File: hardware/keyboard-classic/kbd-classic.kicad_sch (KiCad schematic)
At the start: 19 parts, among them J1 Controller, SW17 Line_Feed, SW32 @(OSI SL), SW34 Rubout (OSI Break), SW61 Power Light, SW9 Caps_Lock

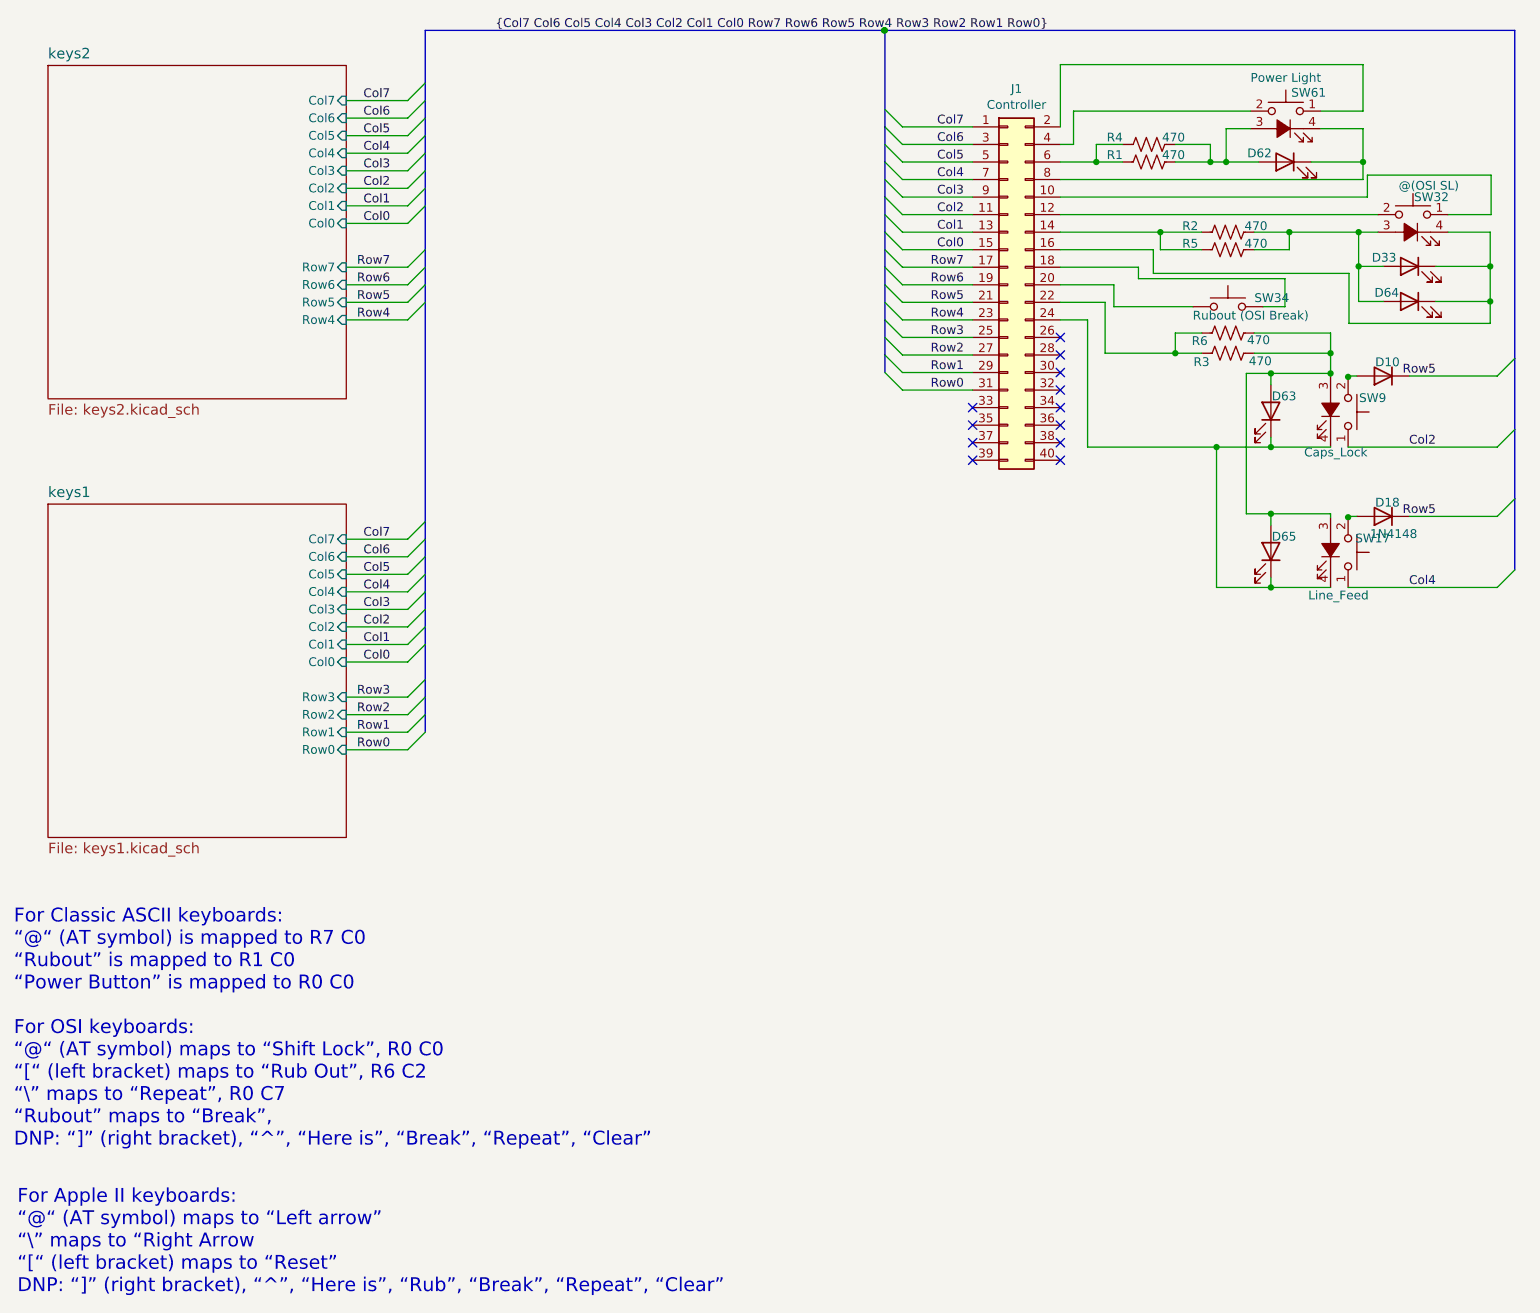
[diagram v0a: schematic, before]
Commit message: Add some mounting hardware
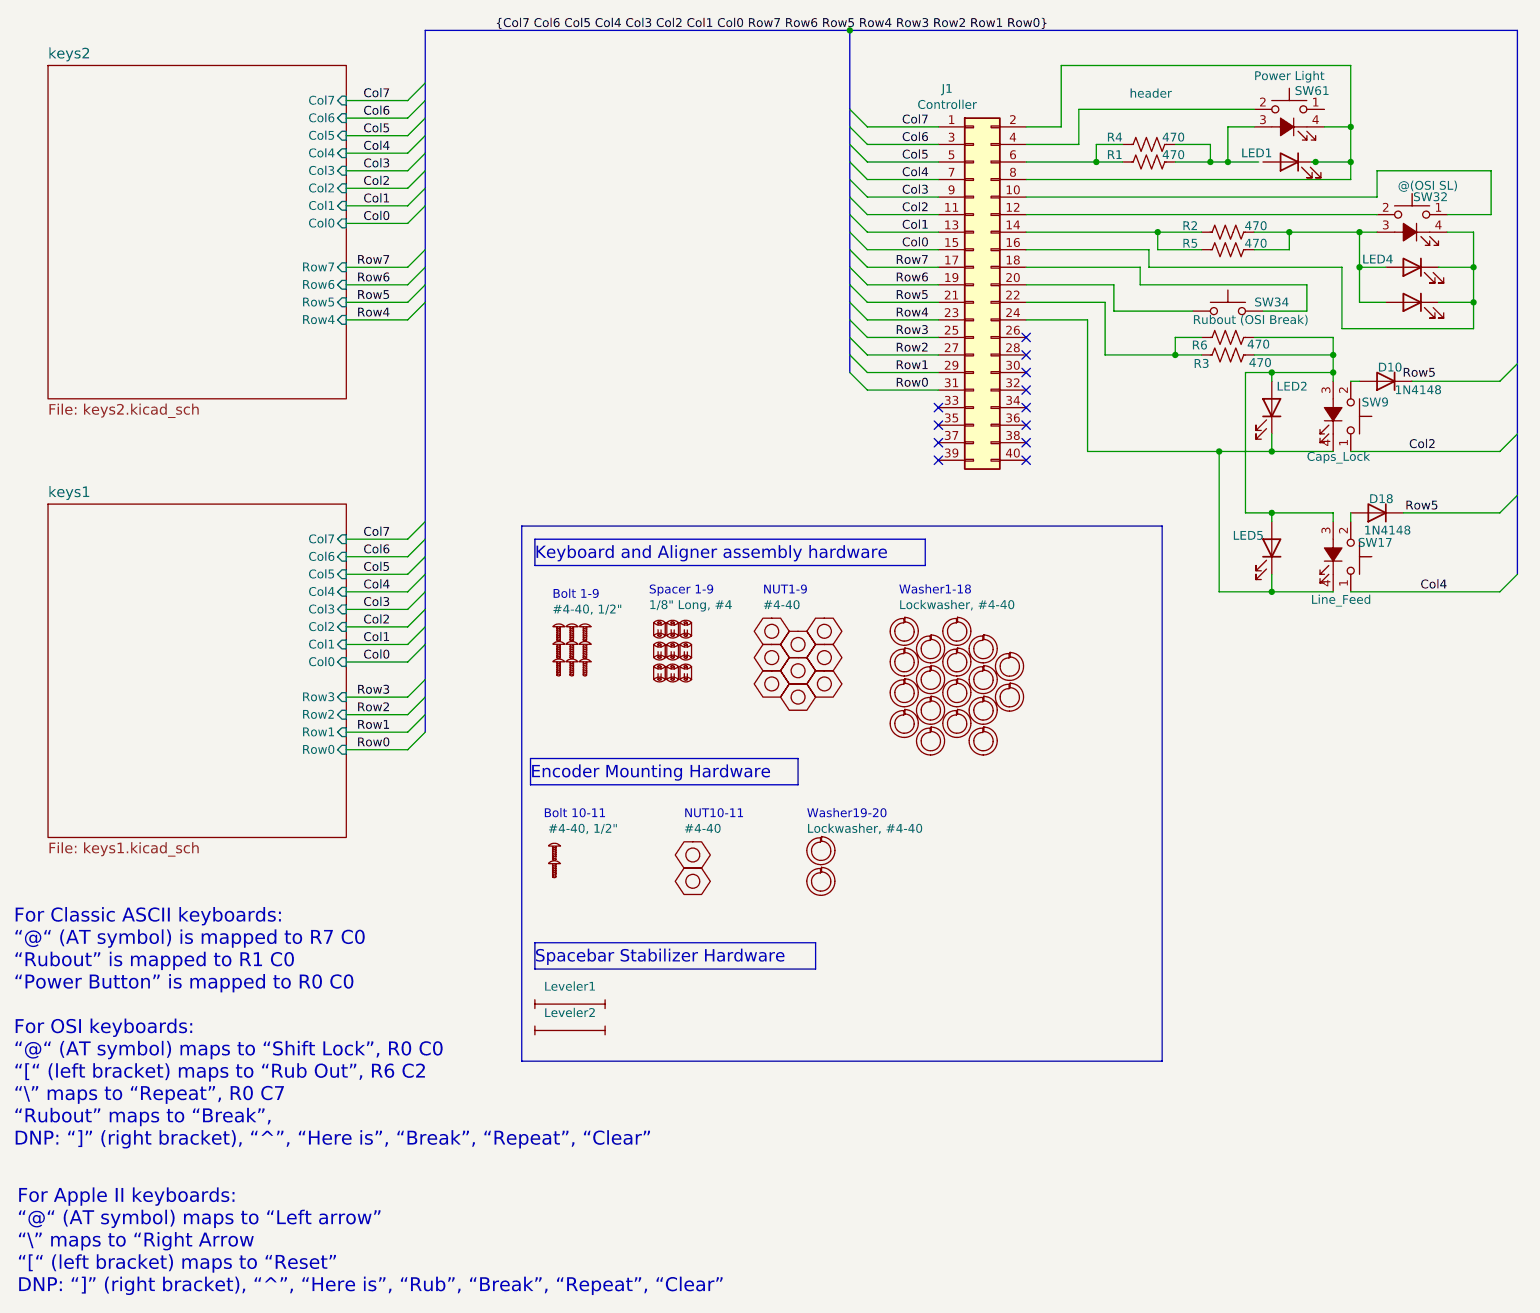
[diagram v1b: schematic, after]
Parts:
- added BOLT1, BOLT10, BOLT11, BOLT2, BOLT3, BOLT4, BOLT5, BOLT6, BOLT7, BOLT8, BOLT9: #4-40, 1/2", symbol mounting-hardware:MNT McMaster Bolt, #4-40, 1/2{dblquote} Long, stainless steel
- added Leveler1, Leveler2: Leveler, symbol unikbd:HW PCB-mount leveling hardware
- added NUT1, NUT10, NUT11, NUT2, NUT3, NUT4, NUT5, NUT6, NUT7, NUT8, NUT9: #4-40, symbol mounting-hardware:MNT McMaster Nut, #4-40, stainless steel
- added SPACER1, SPACER2, SPACER3, SPACER4, SPACER5, SPACER6, SPACER7, SPACER8, SPACER9: Standard Template, symbol mounting-hardware:MNT McMaster Spacer, #4, 3/16{dblquote} OD, 1/8{dblquote} Lon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
- added WASHER1, WASHER10, WASHER11, WASHER12, WASHER13, WASHER14, WASHER15, WASHER16, WASHER17, WASHER18, WASHER19, WASHER2, WASHER20, WASHER3, WASHER4, WASHER5, WASHER6, WASHER7, WASHER8, WASHER9: Lockwasher, #4-40, symbol mounting-hardware:MNT McMaster Lockwasher, #4-40, internal teeth, stainless ste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
- D10: value (none) -> 1N4148; footprint (none) -> unikbd:diode-combined; Manufacturer PN (none) -> MMBD914LT3G
- D18: Manufacturer PN (none) -> MMBD914LT3G
- J1: symbol Connector_Generic:Conn_02x20_Odd_Even -> unikbd:CONN 3M 929975-01-20-RK 40 pin female header, straight, TH, 0.254{dblquote}; Allow Substitution (none) -> Yes; Class (none) -> If applicable; Component Type (none) -> Connector; Component Value (none) -> header; Manufacturer (none) -> 3M; Manufacturer Link (none) -> https://www.3m.com/3M/en_US/p/d/b10419776/; Manufacturer PN (none) -> 929975-01-20-RK; Material (none) -> If applicable; Number of Pins (none) -> 40; Power Rating (none) -> If applicable; RoHS (none) -> Yes; RoHS Document Link (none) -> https://4donline.ihs.com/images/VipMasterIC/IC/IIIM/IIIM-E-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; Standards Version (none) -> 1.1; Temp (Operating) (none) -> -40C/+105C; Temp (Soldering) (none) -> If applicable; Temp (Storage) (none) -> If applicable; Temp Coeff. (none) -> If applicable; Tolerance (none) -> If applicable; Tracking (none) -> No
- LED1: renamed from D62; symbol Device:LED -> unikbd:LED_Lumex_696-SSL-LX3044AD__3mm_amber_THT; Allow Substitution (none) -> Yes; BOM Comment (none) -> Install into switch; Component Type (none) -> LED; Component Value (none) -> Amber; Fitted NO -> YES; Manufacturer (none) -> Lumex; Manufacturer Link (none) -> https://www.lumex.com/datasheet/SSL-LX3044AD; Manufacturer PN (none) -> SSL-LX3044AD; Manufacturer Part Number (none) -> SSL-LX3044AD; Number of Pins (none) -> 2; Package (none) -> T-1 (3mm); Power Rating (none) -> 105mW; RoHS (none) -> Yes; RoHS Document Link (none) -> https://www.mouser.com/catalog/additional/Lumex_6960_RoHS_C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; Standards Version (none) -> 1.1; Temp (Operating) (none) -> -40C/+85C; Tracking (none) -> No
- LED2: renamed from D63; symbol Device:LED -> unikbd:LED_Lumex_696-SSL-LX3044AD__3mm_amber_THT; Allow Substitution (none) -> Yes; BOM Comment (none) -> Install into switch; Component Type (none) -> LED; Component Value (none) -> Amber; Fitted NO -> YES; Manufacturer (none) -> Lumex; Manufacturer Link (none) -> https://www.lumex.com/datasheet/SSL-LX3044AD; Manufacturer PN (none) -> SSL-LX3044AD; Manufacturer Part Number (none) -> SSL-LX3044AD; Number of Pins (none) -> 2; Package (none) -> T-1 (3mm); Power Rating (none) -> 105mW; RoHS (none) -> Yes; RoHS Document Link (none) -> https://www.mouser.com/catalog/additional/Lumex_6960_RoHS_C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; Standards Version (none) -> 1.1; Temp (Operating) (none) -> -40C/+85C; Tracking (none) -> No
- LED3: renamed from D64; symbol Device:LED -> unikbd:LED_Lumex_696-SSL-LX3044AD__3mm_amber_THT; Allow Substitution (none) -> Yes; BOM Comment (none) -> Install into switch; Component Type (none) -> LED; Component Value (none) -> Amber; Fitted NO -> YES; Manufacturer (none) -> Lumex; Manufacturer Link (none) -> https://www.lumex.com/datasheet/SSL-LX3044AD; Manufacturer PN (none) -> SSL-LX3044AD; Manufacturer Part Number (none) -> SSL-LX3044AD; Number of Pins (none) -> 2; Package (none) -> T-1 (3mm); Power Rating (none) -> 105mW; RoHS (none) -> Yes; RoHS Document Link (none) -> https://www.mouser.com/catalog/additional/Lumex_6960_RoHS_C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; Standards Version (none) -> 1.1; Temp (Operating) (none) -> -40C/+85C; Tracking (none) -> No
- LED4: renamed from D33; symbol Device:LED -> unikbd:LED Cree C5SMF-RJE-CT0W0BB2 T1-3/4 5mm Red, 2200 mcd; Allow Substitution (none) -> Yes; BOM Comment (none) -> Install into switch; Component Type (none) -> LED; Component Value (none) -> Amber; Manufacturer (none) -> Lumex; Manufacturer Link (none) -> https://www.lumex.com/datasheet/SSL-LX3044AD; Manufacturer PN (none) -> SSL-LX3044AD; Number of Pins (none) -> 2; Package (none) -> T-1 (3mm); Power Rating (none) -> 105mW; RoHS (none) -> Yes; RoHS Document Link (none) -> https://www.mouser.com/catalog/additional/Lumex_6960_RoHS_C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; Standards Version (none) -> 1.1; Temp (Operating) (none) -> -40C/+85C; Tracking (none) -> No
- LED5: renamed from D65; symbol Device:LED -> unikbd:LED_Lumex_696-SSL-LX3044AD__3mm_amber_THT; Allow Substitution (none) -> Yes; BOM Comment (none) -> Install into switch; Component Type (none) -> LED; Component Value (none) -> Amber; Fitted NO -> YES; Manufacturer (none) -> Lumex; Manufacturer Link (none) -> https://www.lumex.com/datasheet/SSL-LX3044AD; Manufacturer PN (none) -> SSL-LX3044AD; Manufacturer Part Number (none) -> SSL-LX3044AD; Number of Pins (none) -> 2; Package (none) -> T-1 (3mm); Power Rating (none) -> 105mW; RoHS (none) -> Yes; RoHS Document Link (none) -> https://www.mouser.com/catalog/additional/Lumex_6960_RoHS_C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; Standards Version (none) -> 1.1; Temp (Operating) (none) -> -40C/+85C; Tracking (none) -> No
- R4, R5, R6: Manufacturer PN (none) -> ERJ-3EKF3300V
- SW34: symbol Switch:SW_Push -> unikbd:SW Cherry MX/Futaba 1U Style A; Allow Substitution (none) -> Yes; Class (none) -> If applicable; Component Type (none) -> Switch; Component Value (none) -> Key; Manufacturer (none) -> Cherry; Manufacturer Link (none) -> https://www.cherrymx.de/en/cherry-mx/mx-original/mx-black.h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; Manufacturer PN (none) -> MX1A-11NN; Material (none) -> If applicable; Number of Pins (none) -> 2; Power Rating (none) -> 10 mA; RoHS (none) -> Yes; RoHS Document Link (none) -> https://www.mouser.com/catalog/additional/Cherry_Electrical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; Standards Version (none) -> 1.1; Temp (Operating) (none) -> -40C/+170C; Temp (Soldering) (none) -> If applicable; Temp Coeff. (none) -> If applicable; Tolerance (none) -> If applicable; Tracking (none) -> No
- SW61: Fitted NO -> Yes
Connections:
- net Row5: no longer D10.1 (K)
- net at J1.2 (Pin_2): now also J1.8 (Pin_8), LED1.1 (K), SW61.4; no longer SW61.1
- net at R1.1, R4.1, SW61.3: no longer LED1.2 (A)
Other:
- note added: "Bolt 1-9"
- note added: "Bolt 10-11"
- note added: "Encoder Mounting Hardware"
- note added: "Keyboard and Aligner assembly hardware"
- note added: "NUT1-9"
- note added: "NUT10-11"
- note added: "Spacebar Stabilizer Hardware"
- note added: "Spacer 1-9"
- note added: "Washer1-18"
- note added: "Washer19-20"
- moved on the sheet: D10, D18, J1, LED1, LED2, LED5, R6, SW17, SW34, SW61, SW9

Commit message: Update to include mounting hardware
- Fix all components to include full information including BOM
information

- Include all mounting hardware in components List

- fix schematic to align on 0.1" grid.
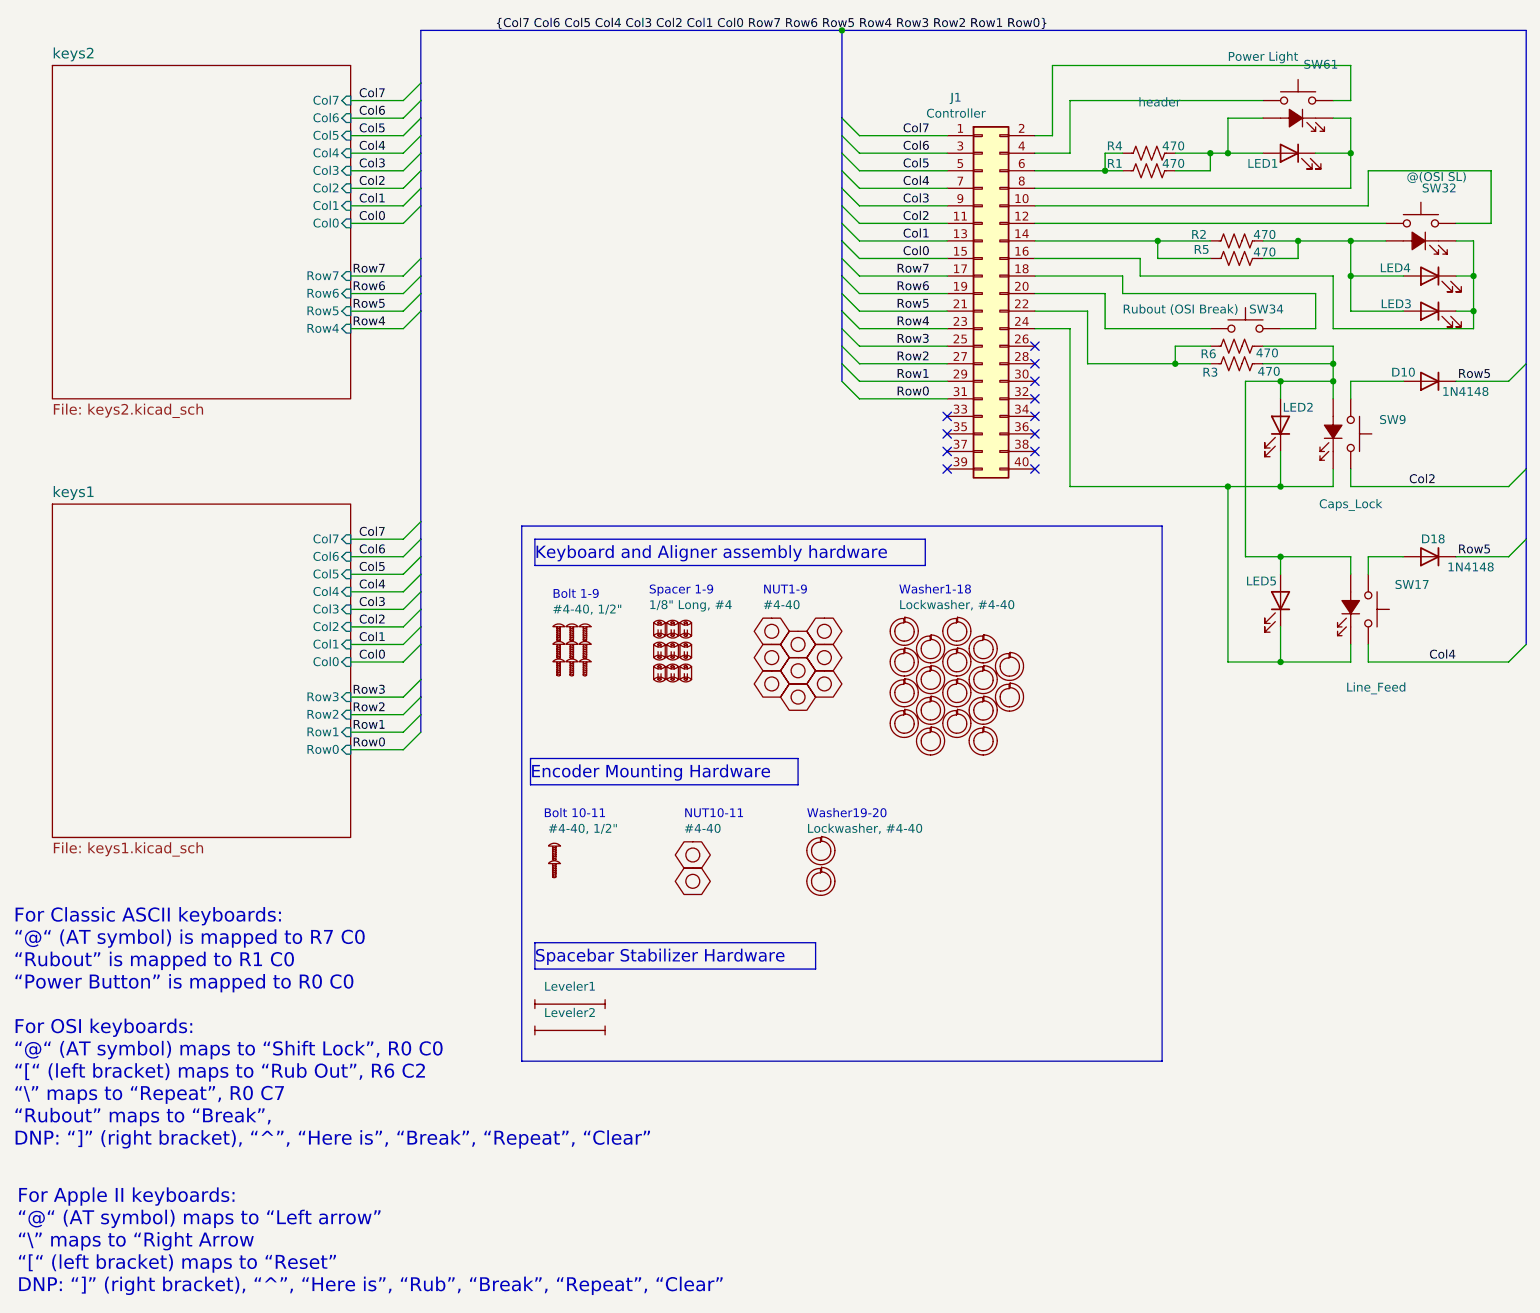
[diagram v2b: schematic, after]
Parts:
- D10, D18: Allow Substitution (none) -> Yes; BOM Comment (none) -> Either SMT or Through-Hole part (1n914 or 1n4148) is fitted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; Class (none) -> If applicable; Component Type (none) -> Diode; Component Value (none) -> 19N14/MMBD914; Fitted YES -> Yes; Manufacturer ON Semiconductor -> Diodes, Inc.; Manufacturer Link (none) -> https://www.diodes.com/part/view/MMBD914; Manufacturer PN MMBD914LT3G -> MMBD914-7-F; Material (none) -> If applicable; Number of Pins (none) -> 3; Package Type (none) -> SOT3-3; Power Rating (none) -> 350 mW / 200 mA; RoHS (none) -> Yes; RoHS Document Link (none) -> https://www.diodes.com/assets/Quality-Reliability-Docs/Mast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; Standards Version (none) -> 1.1; Temp (Operating) (none) -> -65C/150C; Temp (Soldering) (none) -> If applicable; Temp (Storage) (none) -> If applicable; Temp Coeff. (none) -> If applicable; Tolerance (none) -> If applicable; Tracking (none) -> No
- SW17, SW32, SW61, SW9: symbol unikbd:SW_Push_LED -> unikbd:SW Cherry MX/Futaba 1U LED Style A; Allow Substitution (none) -> Yes; Class (none) -> If applicable; Component Type (none) -> Switch; Component Value (none) -> Key; Manufacturer (none) -> Cherry; Manufacturer Link (none) -> https://www.cherrymx.de/en/cherry-mx/mx-original/mx-black.h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; Manufacturer PN (none) -> MX1A-11NN; Material (none) -> If applicable; Number of Pins (none) -> 2; Power Rating (none) -> 10 mA; RoHS (none) -> Yes; RoHS Document Link (none) -> https://www.mouser.com/catalog/additional/Cherry_Electrical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; Standards Version (none) -> 1.1; Temp (Operating) (none) -> -40C/+170C; Temp (Soldering) (none) -> If applicable; Temp Coeff. (none) -> If applicable; Tolerance (none) -> If applicable; Tracking (none) -> No
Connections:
- net Row5: now also D10.1 (K)
- net at J1.8 (Pin_8), LED1.1 (K), SW61.4: no longer J1.2 (Pin_2)
- net at LED1.2 (A): now also R1.1, R4.1, SW61.3
- net at SW61.1: now also J1.2 (Pin_2)
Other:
- moved on the sheet: D10, D18, J1, LED1, LED2, LED4, LED5, R1, R2, R3, R4, R5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
